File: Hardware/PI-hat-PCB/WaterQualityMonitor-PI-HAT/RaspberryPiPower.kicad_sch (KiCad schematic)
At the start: 19 parts, among them IC2 DMMT5401-7-F, Q3 DMG2305UX-7, U5 RT7272AGSP

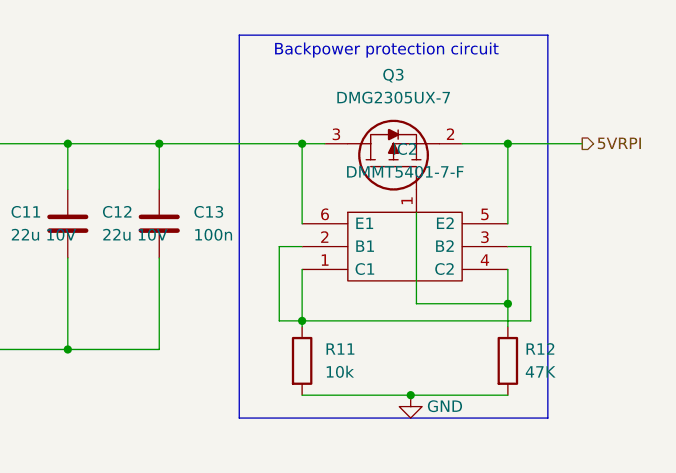
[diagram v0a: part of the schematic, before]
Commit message: changed name from primary (main) to PRI (logical)
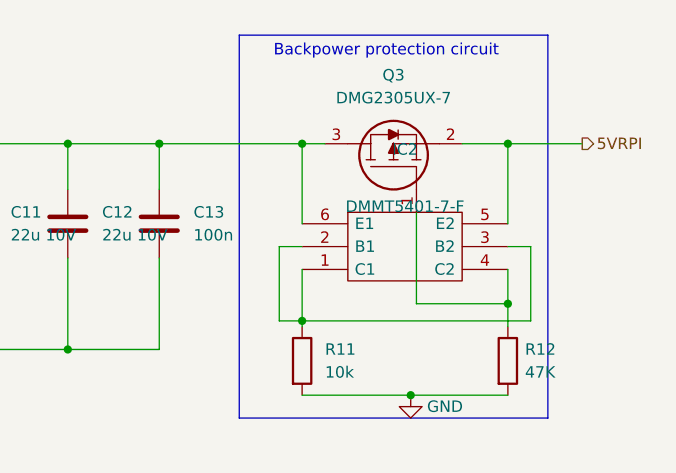
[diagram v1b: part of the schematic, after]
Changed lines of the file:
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@@
   )
   (symbol (lib_id "SamacSys_Parts:DMMT5401-7-F") (at 222.885 102.87 0) (unit 1)
-    (in_bom yes) (on_board yes) (fields_autoplaced)
+    (in_bom yes) (on_board yes)
     (property "Reference" "IC2" (id 0) (at 234.315 94.615 0))
-    (property "Value" "DMMT5401-7-F" (id 1) (at 234.315 97.155 0))
+    (property "Value" "DMMT5401-7-F" (id 1) (at 234.315 100.965 0))
     (property "Footprint" "SmacSYs:SOT95P285X140-6N" (id 2) (at 241.935 100.33 0)
       (effects (font (size 1.27 1.27)) (justify left) hide)

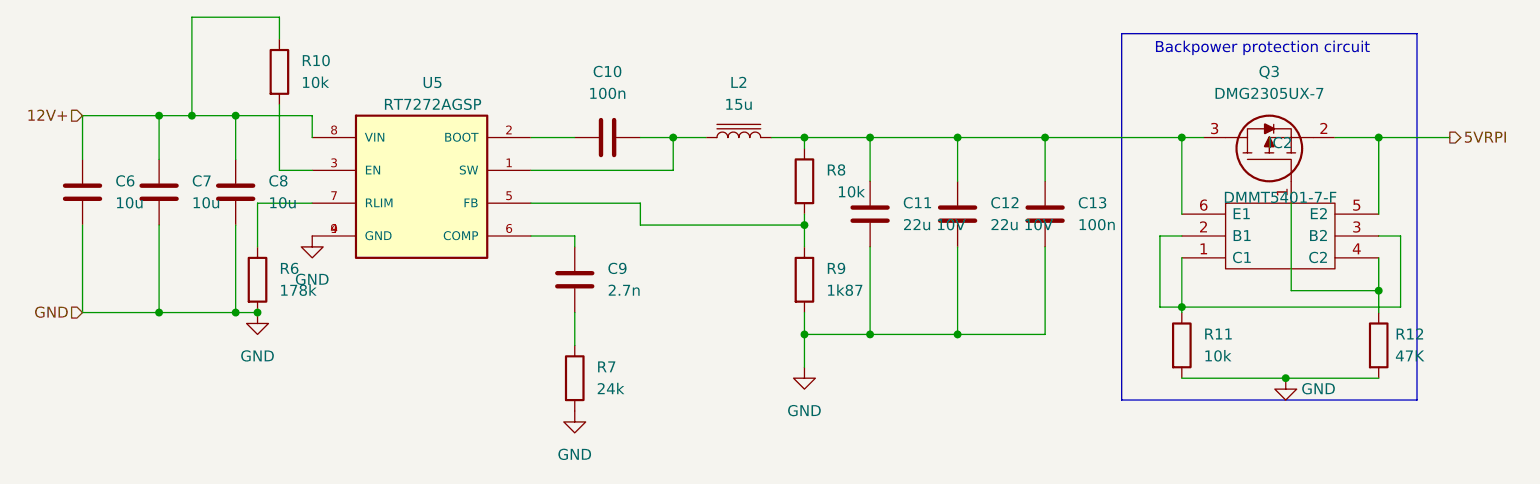
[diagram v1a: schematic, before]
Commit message: enh schematic
added power pins breakout
replaced common ground with specific ground labels
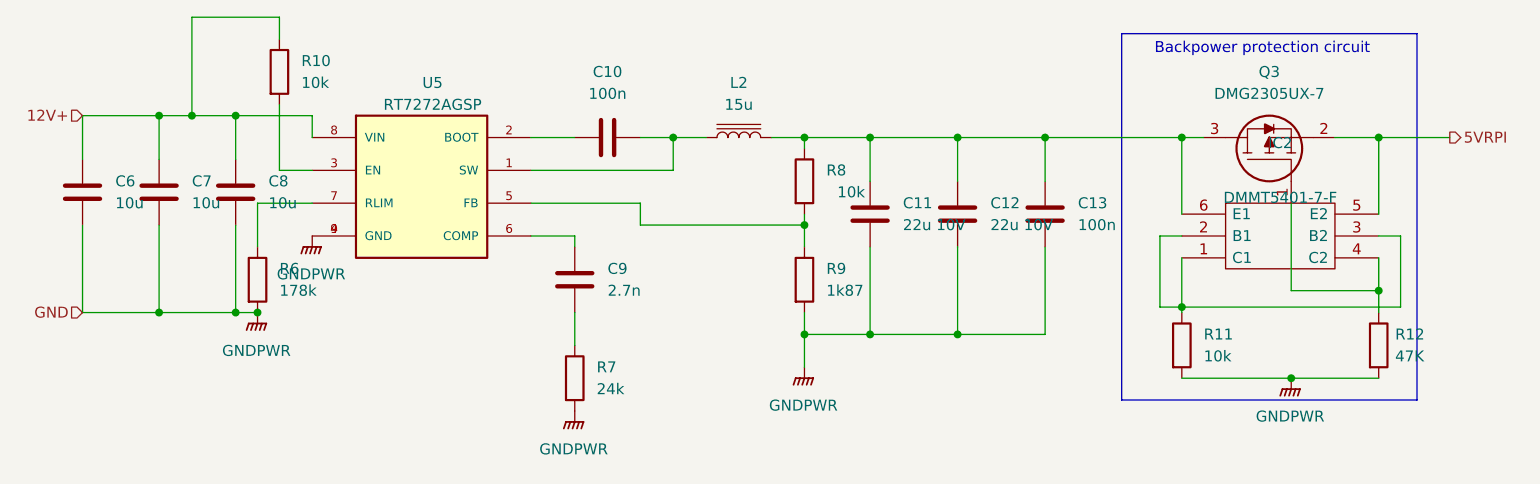
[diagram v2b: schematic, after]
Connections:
- net GND renamed GNDPWR
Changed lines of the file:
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@@
 (kicad_sch (version 20211123) (generator eeschema)
   (paper "A4")
+  (junction (at 104.14 114.3) (diameter 0) (color 0 0 0 0)
+  )
+  (junction (at 245.745 111.76) (diameter 0) (color 0 0 0 0)
+  )
+  (junction (at 179.07 116.84) (diameter 0) (color 0 0 0 0)
+  )
+  (junction (at 179.07 104.14) (diameter 0) (color 0 0 0 0)
+  )
+  (junction (at 113.03 91.44) (diameter 0) (color 0 0 0 0)
+  )
+  (junction (at 196.85 116.84) (diameter 0) (color 0 0 0 0)
+  )
   (junction (at 115.57 114.3) (diameter 0) (color 0 0 0 0)
   )
-  (junction (at 234.95 121.92) (diameter 0) (color 0 0 0 0)
-  )
-  (junction (at 104.14 114.3) (diameter 0) (color 0 0 0 0)
-  )
-  (junction (at 245.745 111.76) (diameter 0) (color 0 0 0 0)
-  )
-  (junction (at 179.07 116.84) (diameter 0) (color 0 0 0 0)
-  )
-  (junction (at 179.07 104.14) (diameter 0) (color 0 0 0 0)
-  )
-  (junction (at 113.03 91.44) (diameter 0) (color 0 0 0 0)
-  )
-  (junction (at 196.85 116.84) (diameter 0) (color 0 0 0 0)
-  )
   (junction (at 104.14 91.44) (diameter 0) (color 0 0 0 0)
   )
@@
   (junction (at 207.01 93.98) (diameter 0) (color 0 0 0 0)
   )
+  (junction (at 235.585 121.92) (diameter 0) (color 0 0 0 0)
+  )
   (junction (at 107.95 91.44) (diameter 0) (color 0 0 0 0)
   )
@@
     (stroke (width 0) (type default) (color 0 0 0 0))
   )
-  (wire (pts (xy 222.885 121.92) (xy 234.95 121.92))
+  (wire (pts (xy 222.885 121.92) (xy 235.585 121.92))
     (stroke (width 0) (type default) (color 0 0 0 0))
   )
@@
     (stroke (width 0) (type default) (color 0 0 0 0))
   )
-  (wire (pts (xy 234.95 121.92) (xy 245.745 121.92))
-    (stroke (width 0) (type default) (color 0 0 0 0))
-  )
   (wire (pts (xy 245.745 105.41) (xy 248.285 105.41))
     (stroke (width 0) (type default) (color 0 0 0 0))
@@
   )
   (wire (pts (xy 152.4 114.3) (xy 152.4 118.11))
+    (stroke (width 0) (type default) (color 0 0 0 0))
+  )
+  (wire (pts (xy 235.585 121.92) (xy 245.745 121.92))
     (stroke (width 0) (type default) (color 0 0 0 0))
   )
@@
     (pin "2")
   )
+  (symbol (lib_id "power:GNDPWR") (at 179.07 120.65 0) (unit 1)
+    (in_bom yes) (on_board yes) (fields_autoplaced)
+    (property "Reference" "#PWR021" (id 0) (at 179.07 125.73 0)
+      (effects (font (size 1.27 1.27)) hide)
+    )
+    (property "Value" "GNDPWR" (id 1) (at 178.943 125.095 0))
+    (property "Footprint" "" (id 2) (at 179.07 121.92 0)
+      (effects (font (size 1.27 1.27)) hide)
+    )
+    (property "Datasheet" "" (id 3) (at 179.07 121.92 0)
+      (effects (font (size 1.27 1.27)) hide)
+    )
+    (pin "1")
+  )
+  (symbol (lib_id "power:GNDPWR") (at 121.92 105.41 0) (unit 1)
+    (in_bom yes) (on_board yes) (fields_autoplaced)
+    (property "Reference" "#PWR019" (id 0) (at 121.92 110.49 0)
+      (effects (font (size 1.27 1.27)) hide)
+    )
+    (property "Value" "GNDPWR" (id 1) (at 121.793 109.855 0))
+    (property "Footprint" "" (id 2) (at 121.92 106.68 0)
+      (effects (font (size 1.27 1.27)) hide)
+    )
+    (property "Datasheet" "" (id 3) (at 121.92 106.68 0)
+      (effects (font (size 1.27 1.27)) hide)
+    )
+    (pin "1")
+  )
   (symbol (lib_id "Device:C") (at 186.69 102.87 180) (unit 1)
     (in_bom yes) (on_board yes) (fields_autoplaced)
@@
     (pin "2")
   )
+  (symbol (lib_id "power:GNDPWR") (at 152.4 125.73 0) (unit 1)
+    (in_bom yes) (on_board yes) (fields_autoplaced)
+    (property "Reference" "#PWR020" (id 0) (at 152.4 130.81 0)
+      (effects (font (size 1.27 1.27)) hide)
+    )
+    (property "Value" "GNDPWR" (id 1) (at 152.273 130.175 0))
+    (property "Footprint" "" (id 2) (at 152.4 127 0)
+      (effects (font (size 1.27 1.27)) hide)
+    )
+    (property "Datasheet" "" (id 3) (at 152.4 127 0)
+      (effects (font (size 1.27 1.27)) hide)
+    )
+    (pin "1")
+  )
   (symbol (lib_id "Device:C") (at 104.14 100.33 0) (unit 1)
     (in_bom yes) (on_board yes) (fields_autoplaced)
@@
     (pin "2")
   )
-  (symbol (lib_id "power:GND") (at 234.95 121.92 0) (unit 1)
-    (in_bom yes) (on_board yes)
-    (property "Reference" "#PWR0116" (id 0) (at 234.95 128.27 0)
-      (effects (font (size 1.27 1.27)) hide)
-    )
-    (property "Value" "GND" (id 1) (at 238.76 123.19 0))
-    (property "Footprint" "" (id 2) (at 234.95 121.92 0)
-      (effects (font (size 1.27 1.27)) hide)
-    )
-    (property "Datasheet" "" (id 3) (at 234.95 121.92 0)
+  (symbol (lib_id "power:GNDPWR") (at 115.57 114.3 0) (unit 1)
+    (in_bom yes) (on_board yes) (fields_autoplaced)
+    (property "Reference" "#PWR018" (id 0) (at 115.57 119.38 0)
+      (effects (font (size 1.27 1.27)) hide)
+    )
+    (property "Value" "GNDPWR" (id 1) (at 115.443 118.745 0))
+    (property "Footprint" "" (id 2) (at 115.57 115.57 0)
+      (effects (font (size 1.27 1.27)) hide)
+    )
+    (property "Datasheet" "" (id 3) (at 115.57 115.57 0)
+      (effects (font (size 1.27 1.27)) hide)
+    )
+    (pin "1")
+  )
+  (symbol (lib_id "power:GNDPWR") (at 235.585 121.92 0) (unit 1)
+    (in_bom yes) (on_board yes) (fields_autoplaced)
+    (property "Reference" "#PWR022" (id 0) (at 235.585 127 0)
+      (effects (font (size 1.27 1.27)) hide)
+    )
+    (property "Value" "GNDPWR" (id 1) (at 235.458 126.365 0))
+    (property "Footprint" "" (id 2) (at 235.585 123.19 0)
+      (effects (font (size 1.27 1.27)) hide)
+    )
+    (property "Datasheet" "" (id 3) (at 235.585 123.19 0)
       (effects (font (size 1.27 1.27)) hide)
     )
@@
     (pin "9")
   )
-  (symbol (lib_id "power:GND") (at 179.07 120.65 0) (unit 1)
-    (in_bom yes) (on_board yes) (fields_autoplaced)
-    (property "Reference" "#PWR0119" (id 0) (at 179.07 127 0)
-      (effects (font (size 1.27 1.27)) hide)
-    )
-    (property "Value" "GND" (id 1) (at 179.07 125.73 0))
-    (property "Footprint" "" (id 2) (at 179.07 120.65 0)
-      (effects (font (size 1.27 1.27)) hide)
-    )
-    (property "Datasheet" "" (id 3) (at 179.07 120.65 0)
-      (effects (font (size 1.27 1.27)) hide)
-    )
-    (pin "1")
-  )
-  (symbol (lib_id "power:GND") (at 121.92 105.41 0) (unit 1)
-    (in_bom yes) (on_board yes) (fields_autoplaced)
-    (property "Reference" "#PWR0115" (id 0) (at 121.92 111.76 0)
-      (effects (font (size 1.27 1.27)) hide)
-    )
-    (property "Value" "GND" (id 1) (at 121.92 110.49 0))
-    (property "Footprint" "" (id 2) (at 121.92 105.41 0)
-      (effects (font (size 1.27 1.27)) hide)
-    )
-    (property "Datasheet" "" (id 3) (at 121.92 105.41 0)
-      (effects (font (size 1.27 1.27)) hide)
-    )
-    (pin "1")
-  )
   (symbol (lib_id "Device:C") (at 152.4 110.49 180) (unit 1)
     (in_bom yes) (on_board yes) (fields_autoplaced)
@@
     (pin "2")
   )
-  (symbol (lib_id "power:GND") (at 152.4 125.73 0) (unit 1)
-    (in_bom yes) (on_board yes) (fields_autoplaced)
-    (property "Reference" "#PWR0118" (id 0) (at 152.4 132.08 0)
-      (effects (font (size 1.27 1.27)) hide)
-    )
-    (property "Value" "GND" (id 1) (at 152.4 130.81 0))
-    (property "Footprint" "" (id 2) (at 152.4 125.73 0)
-      (effects (font (size 1.27 1.27)) hide)
-    )
-    (property "Datasheet" "" (id 3) (at 152.4 125.73 0)
-      (effects (font (size 1.27 1.27)) hide)
-    )
-    (pin "1")
-  )
   (symbol (lib_id "Device:C") (at 156.21 93.98 90) (unit 1)
     (in_bom yes) (on_board yes) (fields_autoplaced)
@@
     (pin "2")
   )
-  (symbol (lib_id "power:GND") (at 115.57 114.3 0) (unit 1)
-    (in_bom yes) (on_board yes) (fields_autoplaced)
-    (property "Reference" "#PWR0117" (id 0) (at 115.57 120.65 0)
-      (effects (font (size 1.27 1.27)) hide)
-    )
-    (property "Value" "GND" (id 1) (at 115.57 119.38 0))
-    (property "Footprint" "" (id 2) (at 115.57 114.3 0)
-      (effects (font (size 1.27 1.27)) hide)
-    )
-    (property "Datasheet" "" (id 3) (at 115.57 114.3 0)
-      (effects (font (size 1.27 1.27)) hide)
-    )
-    (pin "1")
-  )
 )

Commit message: finished up V1.0. Review required
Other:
- company: (none) -> HAN
- title: (none) -> Water Quality Monitor
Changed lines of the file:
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@@
 (kicad_sch (version 20211123) (generator eeschema)
   (paper "A4")
+  (title_block
+    (title "Water Quality Monitor")
+    (rev "1")
+    (company "HAN")
+    (comment 1 "Casper R. Tak")
+  )
   (junction (at 104.14 114.3) (diameter 0) (color 0 0 0 0)
   )
